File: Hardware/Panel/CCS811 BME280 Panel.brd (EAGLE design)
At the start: 93.7 x 93.5 mm, 216 parts, among them J1 JST, J10 JST, J11 PTH, J12 JST, J13 CCS811 Options, J14 JST, J15 PTH, J16 JST, J17 CCS811 Options, J18 JST, J19 PTH, J2 CCS811 Options, J20 JST, J21 CCS811 Options, J22 JST, J23 PTH, J24 JST, J25 CCS811 Options, J26 JST, J27 PTH, J28 JST, J29 CCS811 Options, J3 JST, J30 JST, J31 PTH, J32 JST, J33 CCS811 Options, J34 JST, J35 PTH, J36 JST, J4 PTH, J5 CCS811 Options, J6 JST, J7 PTH, J8 JST, J9 CCS811 Options, U1 CCS811, U11 CCS811, U13 CCS811, U15 CCS811, U17 CCS811, U2 CCS811, U5 CCS811, U7 CCS811, U9 CCS811

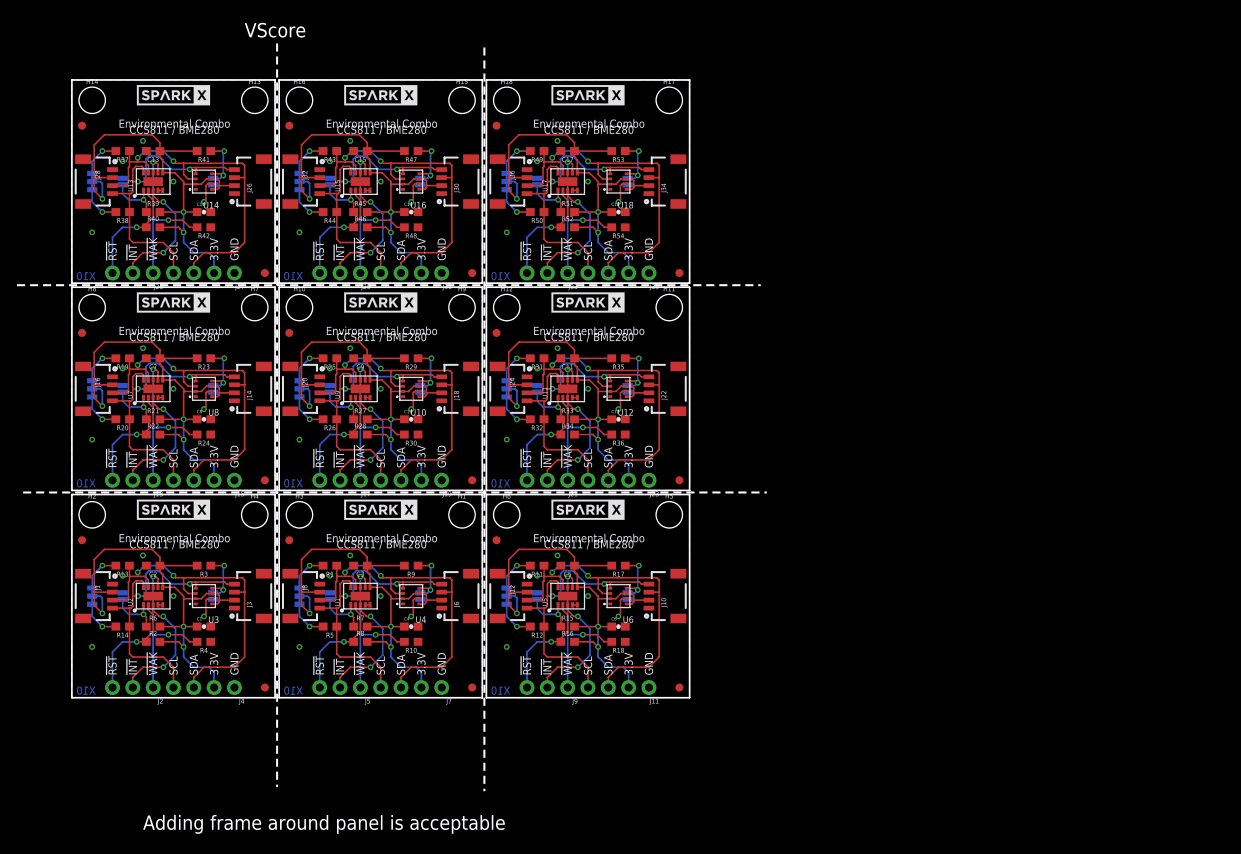
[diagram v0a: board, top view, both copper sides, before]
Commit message: Panel that is now 3x4pcs
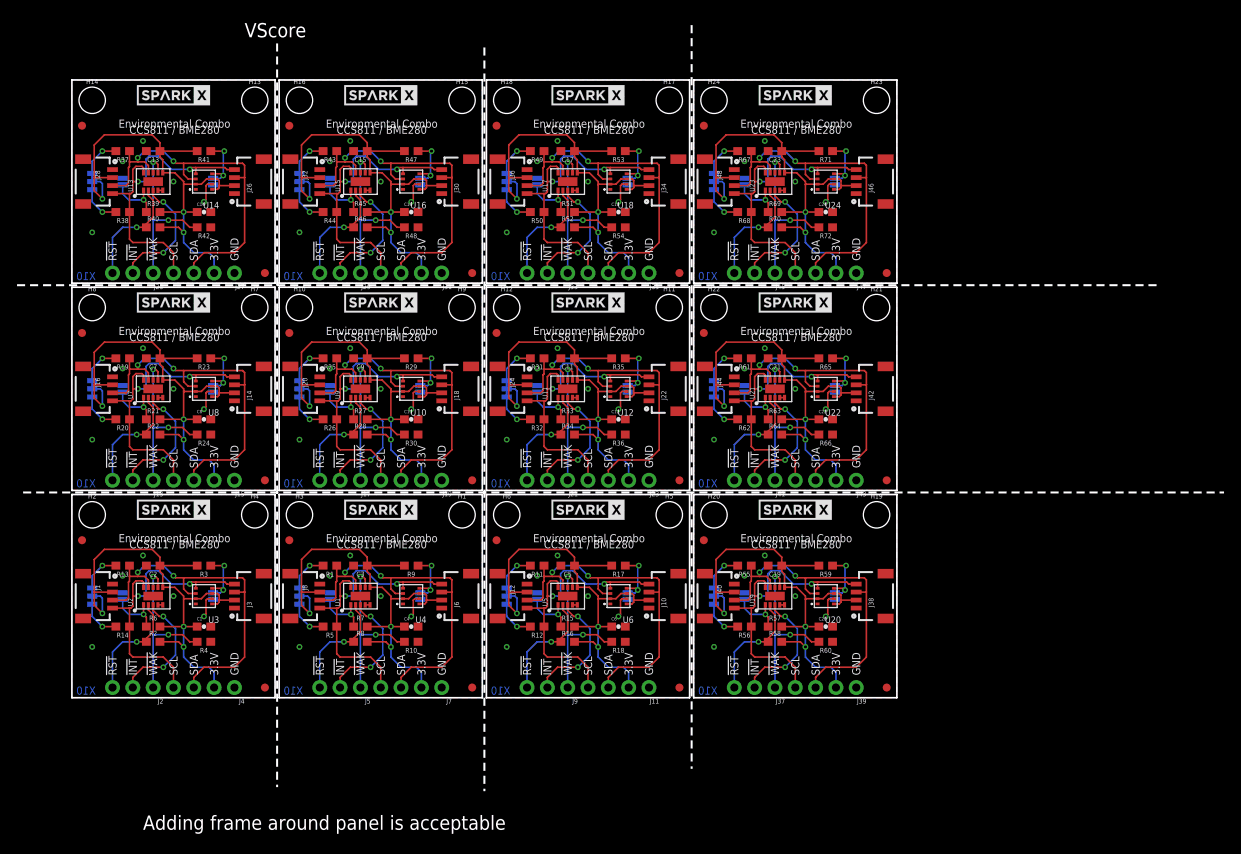
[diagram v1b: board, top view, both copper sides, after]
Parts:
- added ADR19, ADR20, ADR21, ADR22, ADR23, ADR24: (no value), SparkFun-Jumpers:SMT-JUMPER_2_NO_SILK
- added C19, C21, C23: 1.0uF, SparkFun-Capacitors:0603
- added C20, C22, C24: 0.1uF, SparkFun-Capacitors:0603-CAP
- added FD19, FD20, FD21, FD22, FD23, FD24: FIDUCIAL1X2, SparkFun-Aesthetics:FIDUCIAL-1X2
- added H19, H20, H21, H22, H23, H24: STAND-OFF, SparkFun-Hardware:STAND-OFF
- added J37, J41, J45: CCS811 Options, SparkFun-Connectors:1X03_NO_SILK
- added J38, J40, J42, J44, J46, J48: JST, SparkX:1X04_1MM_RA
- added J39, J43, J47: PTH, SparkX:1X04_NO_SILK
- added JP10, JP11, JP12: (no value), SparkFun-Jumpers:SMT-JUMPER_3_2-NC_TRACE_SILK
- added LOGO10, LOGO11, LOGO12: OSHW-LOGOS, SparkFun-Aesthetics:OSHW-LOGO-S
- added R55, R56, R58, R61, R62, R64, R67, R68, R70: 4.7k, SparkFun-Resistors:0603
- added R57, R59, R60, R63, R65, R66, R69, R71, R72: 100k, SparkFun-Resistors:0603
- added U$19, U$20, U$21, U$22, U$23, U$24: SPARKX-LOGO4, SparkX:SPARKX-MEDIUM
- added U19, U21, U23: CCS811, SparkX:LGA10
- added U20, U22, U24: (no value), SparkX:BME280_LGA
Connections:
- new net !INT10: J41.2, U21.3
- new net !INT11: J45.2, U23.3
- new net !INT9: J37.2, U19.3
- new net !RST10: J41.3, R64.1, U21.2
- new net !RST11: J45.3, R70.1, U23.2
- new net !RST9: J37.3, R58.1, U19.2
- new net !WAKE10: J41.1, R66.2, U21.7
- new net !WAKE11: J45.1, R72.2, U23.7
- new net !WAKE9: J37.1, R60.2, U19.7
- new net 3.3V10: C21.1, C22.1, J42.2, J43.2, J44.2, JP11.2, R63.2, R64.2, R65.2, U21.6, U22.2, U22.6, U22.8
- new net 3.3V11: C23.1, C24.1, J46.2, J47.2, J48.2, JP12.2, R69.2, R70.2, R71.2, U23.6, U24.2, U24.6, U24.8
- new net 3.3V9: C19.1, C20.1, J38.2, J39.2, J40.2, JP10.2, R57.2, R58.2, R59.2, U19.6, U20.2, U20.6, U20.8
- new net CCS811_ADDR10: ADR21.2, R63.1, U21.1
- new net CCS811_ADDR11: ADR23.2, R69.1, U23.1
- new net CCS811_ADDR9: ADR19.2, R57.1, U19.1
- new net GND10: ADR21.1, ADR22.1, C21.2, C22.2, J42.1, J43.1, J44.1, R66.1, U21.EP, U22.1, U22.7
- new net GND11: ADR23.1, ADR24.1, C23.2, C24.2, J46.1, J47.1, J48.1, R72.1, U23.EP, U24.1, U24.7
- new net GND9: ADR19.1, ADR20.1, C19.2, C20.2, J38.1, J39.1, J40.1, R60.1, U19.EP, U20.1, U20.7
- new net N$19: JP10.3, R55.2
- new net N$20: JP10.1, R56.2
- new net N$21: JP11.3, R61.2
- new net N$22: JP11.1, R62.2
- new net N$23: JP12.3, R67.2
- new net N$24: JP12.1, R68.2
- new net NTC_SENSE10: U21.4, U21.5
- new net NTC_SENSE11: U23.4, U23.5
- new net NTC_SENSE9: U19.4, U19.5
- new net SCL10: J42.4, J43.4, J44.4, R62.1, U21.10, U22.4
- new net SCL11: J46.4, J47.4, J48.4, R68.1, U23.10, U24.4
- new net SCL9: J38.4, J39.4, J40.4, R56.1, U19.10, U20.4
- new net SDA10: J42.3, J43.3, J44.3, R61.1, U21.9, U22.3
- new net SDA11: J46.3, J47.3, J48.3, R67.1, U23.9, U24.3
- new net SDA9: J38.3, J39.3, J40.3, R55.1, U19.9, U20.3
- new net SDO/ADR10: ADR22.2, R65.1, U22.5
- new net SDO/ADR11: ADR24.2, R71.1, U24.5
- new net SDO/ADR9: ADR20.2, R59.1, U20.5
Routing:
- net 3.3V9: track 0.00 -> 64.1 mm, vias 0 -> 3
- net 3.3V11: track 0.00 -> 64.1 mm, vias 0 -> 3
- net 3.3V10: track 0.00 -> 64.1 mm, vias 0 -> 3
- net SDA9: track 0.00 -> 47.3 mm, vias 0 -> 2
- net SDA10: track 0.00 -> 47.3 mm, vias 0 -> 2
- net SDA11: track 0.00 -> 47.3 mm, vias 0 -> 2
- net SCL11: track 0.00 -> 39.2 mm, vias 0 -> 2
- net SCL10: track 0.00 -> 39.2 mm, vias 0 -> 2
- net SCL9: track 0.00 -> 39.2 mm, vias 0 -> 2
- net !WAKE11: track 0.00 -> 21.8 mm, vias 0 -> 2
- net !WAKE9: track 0.00 -> 21.8 mm, vias 0 -> 2
- net !WAKE10: track 0.00 -> 21.8 mm, vias 0 -> 2
- net !INT10: track 0.00 -> 15.5 mm, vias 0 -> 2
- net !INT9: track 0.00 -> 15.5 mm, vias 0 -> 2
- net !INT11: track 0.00 -> 15.5 mm, vias 0 -> 2
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- added copper zone on layer 1, net GND10
- added copper zone on layer 16, net GND10
- added copper zone on layer 1, net GND11
- added copper zone on layer 16, net GND11
- added copper zone on layer 1, net GND9
- added copper zone on layer 16, net GND9
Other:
- board size 93.7 x 93.5 mm -> 150.9 x 95.8 mm
